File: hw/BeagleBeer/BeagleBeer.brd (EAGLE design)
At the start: 71.8 x 54.6 mm, 96 parts

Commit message: Route BeagleBeer Flying Squirrel Controller PCB.
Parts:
- removed C8: 0.1 uF, geoffculp:0805
- removed U$42: CAT24C256WI-GT3, ON Semiconductor_By_element14_Batch_1:SOIC127P600X175-8N
- removed U$7: TEMPERATURE-SENSORUMAX8, geoffculp:UMAX8
- added R35, R36, R37, R38: 10K, geoffculp:0805
- added U1: TEMPERATURE-SENSORUMAX8, geoffculp:UMAX8
- added U5: CAT24C256WI-GT3, ON Semiconductor_By_element14_Batch_1:SOIC127P600X175-8N
- U$2: value BEAGLEBONE_OUTLINE -> BEAGLEBONE_OUTLINEBEAGLEBEER; device microbuilder:BEAGLEBONE_SHIELD -> adafruit:BEAGLEBEER_SHIELD
- moved C16 458.8 mm to (-13.0, 68.3), turned to 90 degrees
- moved C15 457.9 mm to (-2.79, 68.1), turned to 90 degrees
- moved TP2 448.2 mm to (41.4, 32.0)
- moved R34 437.1 mm to (34.8, 27.2), turned to 180 degrees
- moved U4 421.1 mm to (-7.62, 63.8), turned to 270 degrees
- moved C12 398.6 mm to (-28.4, 23.4), turned to 270 degrees
- moved C14 394.9 mm to (-28.2, 13.0), turned to 270 degrees
- moved C11 393.1 mm to (-38.4, 23.4), turned to 270 degrees
- moved C2 391.8 mm to (52.1, 32.3)
- moved C13 389.6 mm to (-37.6, 13.0), turned to 270 degrees
- moved U2 365.8 mm to (-33.5, 28.2), turned to 90 degrees
- moved U3 362.5 mm to (-33.0, 17.0), turned to 90 degrees
- moved TEST_C 351.0 mm to (-3.05, 109.5)
- moved HEADER-RJ4 328.5 mm to (-53.8, 88.1), turned to 270 degrees
- moved TEST_D 321.0 mm to (-3.30, 104.1)
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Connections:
- removed net AVCC: C7.1, JP1.4, U$2.39
- removed net I2C1_SCA: U$42.5
- removed net I2C1_SCL: JP3.15, U$2.63
- removed net N$104: U4.9
- removed net N$105: U4.8
- removed net N$11: JP1.13, U$2.21
- removed net N$12: JP1.12, U$2.23
- removed net N$13: JP1.11, U$2.25
- removed net N$14: JP1.10, U$2.27
- removed net N$15: JP1.9, U$2.29
- removed net N$21: JP1.3, U$2.41
- removed net N$22: JP1.2, U$2.43
- removed net N$23: JP1.1, U$2.45
- removed net N$24: R19.1
- removed net N$29: JP2.6, U$2.12
- removed net N$30: JP2.7, U$2.14
- removed net N$31: JP2.8, U$2.16
- removed net N$32: JP2.9, U$2.18
- removed net N$43: JP2.20, U$2.40
- removed net N$44: JP2.21, U$2.42
- removed net N$47: JP1.22, U$2.3
- removed net N$48: JP1.21, U$2.5
- removed net N$56: JP3.14, U$2.65
- removed net N$58: JP3.12, U$2.69
- removed net N$59: JP3.11, U$2.71
- removed net N$6: JP1.18, U$2.11
- removed net N$78: JP4.9, U$2.64
- removed net N$79: JP4.10, U$2.66
- removed net N$8: JP1.16, U$2.15
- removed net N$9: JP1.15, U$2.17
- removed net VCC: U$42.4
- new net ALARM_3P3: JP3.12, U$2.69, U4.8
- new net EEPROM_SCA: U5.5
- new net EEPROM_SCL: JP3.15, R36.1, U$2.63, U5.6
- new net EEPROM_SDA: JP4.9, R38.1, U$2.64
- new net LCD_SCL: JP3.14, R35.1, U$2.65
- new net LCD_SDA: JP4.10, R37.1, U$2.66
- new net RESET_3P3: JP3.11, U$2.71, U4.9
- net 3.3V: now also C2.1, C6.1, C7.1, R35.2, R36.2, R37.2, R38.2, U5.4; no longer C8.1
- net 5V: now also R19.1
- net BUZZER_3P3: now also JP1.10, U$2.27
- net FLOW_C: no longer U2.17
- net FLOW_C_3P3: now also JP2.6, U$2.12; no longer U2.4
- net FLOW_D: no longer U2.16
- net FLOW_D_3P3: now also JP2.7, U$2.14; no longer U2.5
- net GND: now also U1.4, U5.1, U5.2, U5.3, U5.8; no longer C8.2, U$42.2, U$42.8, U$7.4
- net GPIO_A_3P3: now also JP1.15, U$2.17
- net GPIO_B_3P3: now also JP1.13, U$2.21
- net GPIO_C_3P3: now also JP1.12, U$2.23
- net GPIO_D_3P3: now also JP1.11, U$2.25
- net GPIO_E: no longer U4.12
- net LED_FLOW_A: no longer U2.15
- net LED_FLOW_A_3P3: now also JP2.8, U$2.16; no longer U2.6
- net LED_FLOW_B: no longer U2.14
- net LED_FLOW_B_3P3: now also JP2.9, U$2.18; no longer U2.7
- net LED_FLOW_C_3P3: now also JP2.20, U$2.40
- net LED_FLOW_D_3P3: now also JP2.21, U$2.42
- net N$102: now also TP2.TP, U5.7; no longer U$42.7
- net ONEWIRE_A: now also U1.1; no longer U$7.1
- net ONEWIRE_A_3P3: now also JP1.22, U$2.3
- net ONEWIRE_B_3P3: now also JP1.21, U$2.5
- net ONEWIRE_C_3P3: now also JP1.18, U$2.11
- net ONEWIRE_D_3P3: now also JP1.16, U$2.15
- net RELAY_A_3P3: now also JP1.4, U$2.39
- net RELAY_B_3P3: now also JP1.3, U$2.41
- net RELAY_C_3P3: now also JP1.2, U$2.43
- net RELAY_D_3P3: now also JP1.1, U$2.45
- net RESET: now also U4.12
- net TEST_PULSE_3P3: now also JP1.9, U$2.29
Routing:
- net GND: track 0.00 -> 617.9 mm, vias 0 -> 16
- net 5V: track 0.00 -> 478.2 mm, vias 0 -> 11
- net 3.3V: track 0.00 -> 298.6 mm, vias 0 -> 14
- net FLOW_A: track 0.00 -> 148.4 mm, vias 0 -> 2
- net FLOW_B: track 0.00 -> 147.2 mm, vias 0 -> 2
- net GPIO_C: track 0.00 -> 146.2 mm, vias 0 -> 2
- net LED_FLOW_D: track 0.00 -> 140.5 mm, vias 0 -> 2
- net LED_FLOW_C: track 0.00 -> 133.5 mm
- net RESET_3P3: track 0.00 -> 126.4 mm, vias 0 -> 2
- net FLOW_D: track 0.00 -> 111.1 mm, vias 0 -> 1
- net ONEWIRE_D: track 0.00 -> 110.7 mm, vias 0 -> 2
- net FLOW_C: track 0.00 -> 109.0 mm, vias 0 -> 1
- net ONEWIRE_C: track 0.00 -> 105.8 mm, vias 0 -> 1
- net ONEWIRE_A: track 0.00 -> 88.3 mm, vias 0 -> 5
- net GPIO_A: track 0.00 -> 84.5 mm, vias 0 -> 2
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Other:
- board size 71.8 x 54.6 mm -> 130.8 x 118.7 mm
- board text added: "February 2013 Made in the USA"
- board text added: "Flying Squirrel Controller"
- board text removed: "10"
- board text removed: "11"
- board text removed: "12"
- board text removed: "13"
- board text removed: "14"
- board text removed: "15"
- board text removed: "16"
- board text removed: "17"
- board text removed: "18"
- board text removed: "19"
- board text removed: "2"
- board text removed: "20"
- board text removed: "21"
- board text removed: "22"
- board text removed: "23"
- board text removed: "24"
- board text removed: "25"
- board text removed: "26"
- board text removed: "27"
- board text removed: "28"
- board text removed: "29"
- board text removed: "3"
- board text removed: "30"
- board text removed: "31"
- board text removed: "32"
- board text removed: "33"
- board text removed: "34"
- board text removed: "35"
- board text removed: "36"
- board text removed: "37"
- board text removed: "38"
- board text removed: "39"
- board text removed: "40"
- board text removed: "41"
- board text removed: "42"
- board text removed: "43"
- board text removed: "44"
- board text removed: "4\"
- board text removed: "5"
- board text removed: "6"
- board text removed: "7"
- board text removed: "8"
- board text removed: "9"
- board text removed: "P8"
- board text removed: "P9"

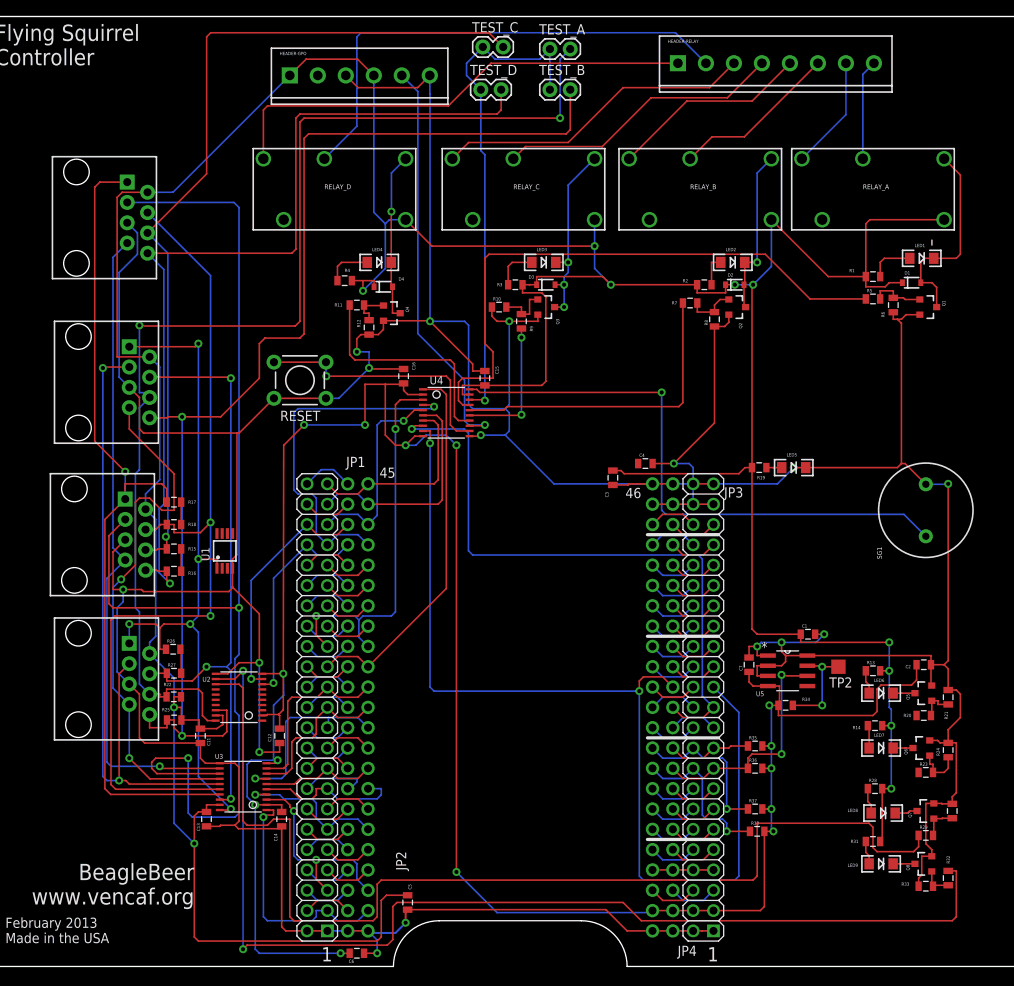
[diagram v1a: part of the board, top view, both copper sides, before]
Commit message: Run ERC on Controller and reroute.
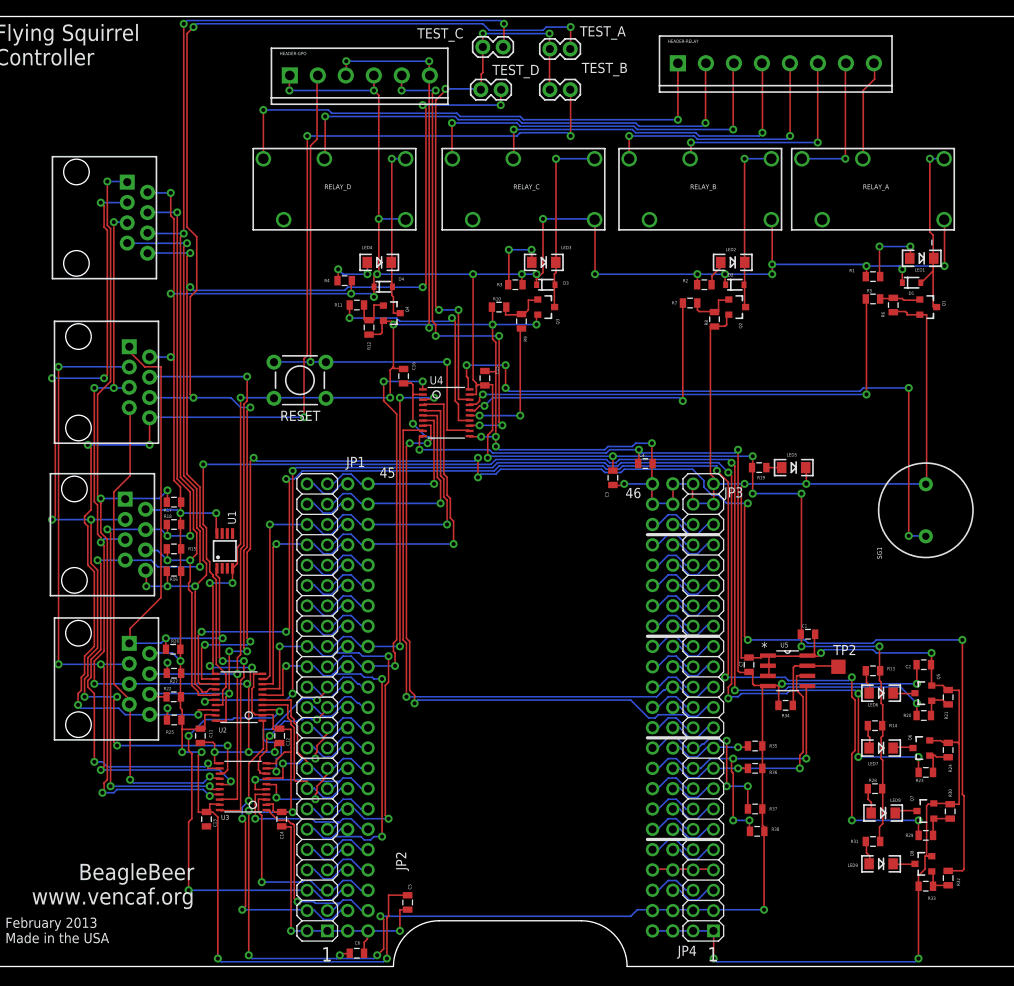
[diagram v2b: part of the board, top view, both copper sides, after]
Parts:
- moved R30 0.26 mm to (55.4, 13.9)
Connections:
- removed net EEPROM_SCA: U5.5
- removed net GPIO_E: HEADER-GPO.2
- removed net N$2: R26.2, R27.2
- removed net N$20: R17.2, R18.2
- removed net N$3: R15.2, R16.2
- removed net N$37: JP2.14, U$2.28
- removed net N$38: JP2.15, U$2.30
- removed net N$50: JP2.2, U$2.4
- removed net N$68: JP2.3, U$2.6
- new net FLOW_A_3P3: JP2.2, U$2.4, U2.1
- net 3.3V: now also C4.1
- net 5V: now also R15.2, R16.2, R17.2, R18.2, R26.2, R27.2, U1.8
- net EEPROM_SDA: now also U5.5
- net FLOW_B_3P3: now also JP2.3, U$2.6
- net FLOW_C: now also U2.15
- net FLOW_C_3P3: now also JP2.14, U$2.28, U2.6
- net FLOW_D: now also U2.14
- net FLOW_D_3P3: now also JP2.15, U$2.30, U2.7
- net LED_FLOW_A: now also U2.17
- net LED_FLOW_A_3P3: now also U2.4
- net LED_FLOW_B: now also U2.16
- net LED_FLOW_B_3P3: now also U2.5
- net RESET: now also HEADER-GPO.2
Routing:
- net LED_FLOW_B: track 0.00 -> 159.3 mm, vias 0 -> 8
- net LED_FLOW_A: track 0.00 -> 153.0 mm, vias 0 -> 4
- net FLOW_B_3P3: track 0.00 -> 55.6 mm, vias 0 -> 3
- net RESET_3P3: track 126.4 -> 75.9 mm, vias 2 -> 1
- net FLOW_D_3P3: track 6.13 -> 56.2 mm, vias 0 -> 3
- net FLOW_C_3P3: track 6.13 -> 53.9 mm, vias 0 -> 3
- net FLOW_A_3P3: track 0.00 -> 39.5 mm, vias 0 -> 3
- net LED_FLOW_D: track 140.5 -> 178.4 mm, vias 2 -> 8
- net RESET: track 32.3 -> 69.2 mm, vias 1 -> 2
- net GND: track 617.9 -> 581.1 mm, vias 16 -> 34
- net GPIO_C: track 146.2 -> 111.1 mm, vias 2 -> 9
- net FLOW_C: track 109.0 -> 143.6 mm, vias 1 -> 5
- net LED_FLOW_C: track 133.5 -> 165.4 mm, vias 0 -> 8
- net 3.3V: track 298.6 -> 269.6 mm, vias 14 -> 13
- net FLOW_D: track 111.1 -> 138.9 mm, vias 1 -> 8
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
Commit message: Clean up Gerber files.  Generate XY parts placement files.
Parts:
- moved C12 65.3 mm to (36.6, 28.8)
- moved C16 65.3 mm to (52.1, 73.8)
- moved C2 65.3 mm to (117.1, 37.7)
- moved C4 65.3 mm to (82.3, 62.9)
- moved D1 65.3 mm to (115.6, 85.5)
- moved D2 65.3 mm to (93.5, 85.2)
- moved D3 65.3 mm to (69.9, 85.2)
- moved D4 65.3 mm to (49.6, 85.0)
- moved JP1 65.3 mm to (47.7, 32.4)
- moved JP2 65.3 mm to (45.1, 32.4)
- moved JP3 65.3 mm to (85.8, 32.4)
- moved LED5 65.3 mm to (100.9, 62.4)
- moved LED6 65.3 mm to (111.8, 34.2)
- moved LED7 65.3 mm to (111.8, 27.3)
- moved LED8 65.3 mm to (112.1, 19.2)
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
